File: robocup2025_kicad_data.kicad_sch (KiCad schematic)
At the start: 2 parts, among them U1 RASPBERRY_PI_4B_4GB, U2 ESP32-DEVKITC-32E

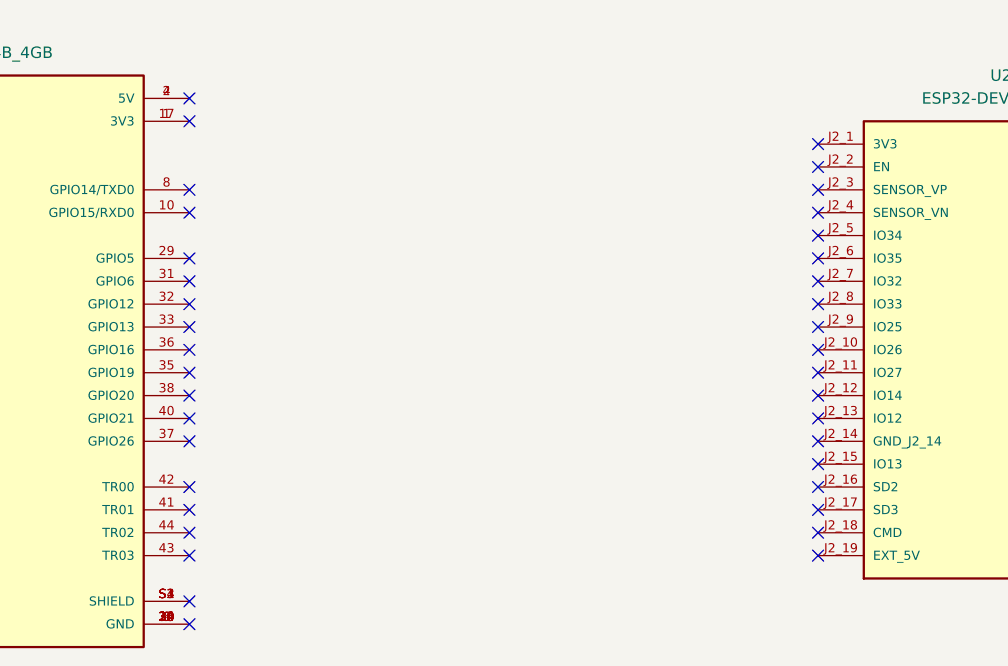
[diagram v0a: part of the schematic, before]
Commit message: robocup2025_kicad_data.kicad_sch: End of the day
ERC Failing
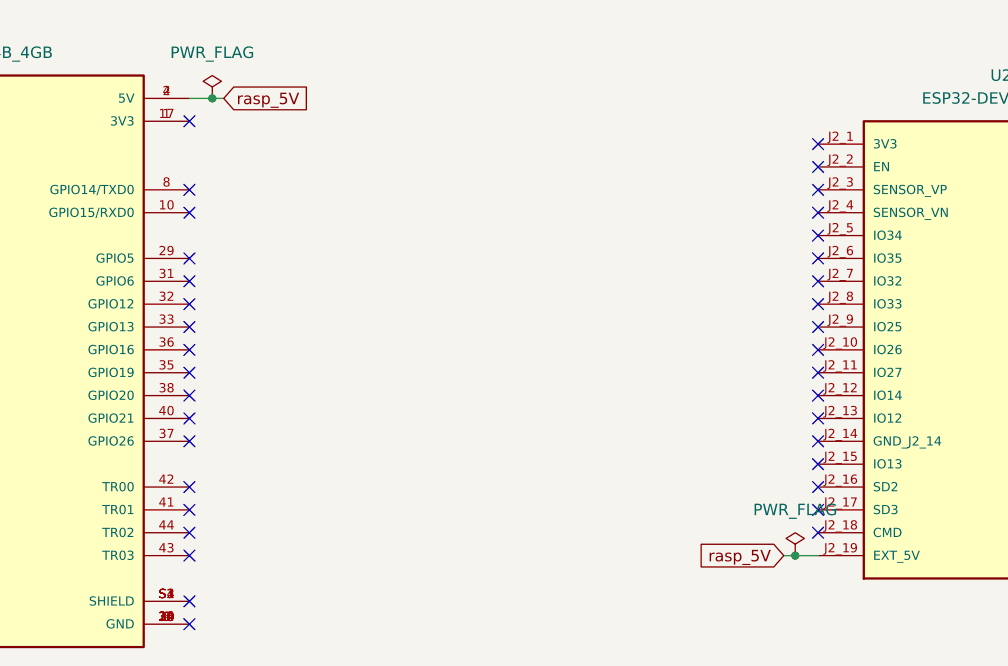
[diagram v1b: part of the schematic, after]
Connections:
- net rasp_5V: now reaches U1.2 (5V), U1.4 (5V)
- net rasp_5V: now also U2.J2_19 (EXT_5V)
- no-connect marks 70 -> 68
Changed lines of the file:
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@@
 	(generator_version "8.0")
 	(paper "A4")
+	(junction
+		(at 147.32 83.82)
+		(diameter 0)
+		(color 0 0 0 0)
+	)
+	(junction
+		(at 82.55 33.02)
+		(diameter 0)
+		(color 0 0 0 0)
+	)
 	(no_connect
 		(at 80.01 66.04)
@@
 	)
 	(no_connect
-		(at 149.86 83.82)
-	)
-	(no_connect
 		(at 80.01 35.56)
 	)
@@
 	(no_connect
 		(at 80.01 58.42)
-	)
-	(no_connect
-		(at 80.01 33.02)
 	)
 	(no_connect
@@
 	(wire
 		(pts
-			(xy 25.4 38.1) (xy 29.21 38.1)
+			(xy 82.55 33.02) (xy 83.82 33.02)
 		)
 		(stroke
@@
 	(wire
 		(pts
-			(xy 190.5 43.18) (xy 194.31 43.18)
+			(xy 25.4 38.1) (xy 29.21 38.1)
 		)
 		(stroke
 			(width 0)
 			(type default)
+		)
+	)
+	(wire
+		(pts
+			(xy 146.05 83.82) (xy 147.32 83.82)
+		)
+		(stroke
+			(width 0)
+			(type default)
+		)
+	)
+	(wire
+		(pts
+			(xy 190.5 43.18) (xy 194.31 43.18)
+		)
+		(stroke
+			(width 0)
+			(type default)
+		)
+	)
+	(wire
+		(pts
+			(xy 147.32 83.82) (xy 149.86 83.82)
+		)
+		(stroke
+			(width 0)
+			(type default)
+		)
+	)
+	(wire
+		(pts
+			(xy 80.01 33.02) (xy 82.55 33.02)
+		)
+		(stroke
+			(width 0)
+			(type default)
+		)
+	)
+	(global_label "rasp_5V"
+		(shape input)
+		(at 146.05 83.82 180)
+		(fields_autoplaced yes)
+		(effects
+			(font
+				(size 1.27 1.27)
+			)
+			(justify right)
+		)
+		(property "Intersheetrefs" "${INTERSHEET_REFS}"
+			(at 135.6868 83.82 0)
+			(effects
+				(font
+					(size 1.27 1.27)
+				)
+				(justify right)
+				(hide yes)
+			)
+		)
+	)
+	(global_label "rasp_5V"
+		(shape input)
+		(at 83.82 33.02 0)
+		(fields_autoplaced yes)
+		(effects
+			(font
+				(size 1.27 1.27)
+			)
+			(justify left)
+		)
+		(property "Intersheetrefs" "${INTERSHEET_REFS}"
+			(at 94.1832 33.02 0)
+			(effects
+				(font
+					(size 1.27 1.27)
+				)
+				(justify left)
+				(hide yes)
+			)
 		)
 	)
@@
 				(justify right)
 				(hide yes)
+			)
+		)
+	)
+	(symbol
+		(lib_id "power:PWR_FLAG")
+		(at 147.32 83.82 0)
+		(unit 1)
+		(exclude_from_sim no)
+		(in_bom yes)
+		(on_board yes)
+		(dnp no)
+		(fields_autoplaced yes)
+		(property "Reference" "#FLG2"
+			(at 147.32 81.915 0)
+			(effects
+				(font
+					(size 1.27 1.27)
+				)
+				(hide yes)
+			)
+		)
+		(property "Value" "PWR_FLAG"
+			(at 147.32 78.74 0)
+			(effects
+				(font
+					(size 1.27 1.27)
+				)
+			)
+		)
+		(property "Footprint" ""
+			(at 147.32 83.82 0)
+			(effects
+				(font
+					(size 1.27 1.27)
+				)
+				(hide yes)
+			)
+		)
+		(property "Datasheet" "~"
+			(at 147.32 83.82 0)
+			(effects
+				(font
+					(size 1.27 1.27)
+				)
+				(hide yes)
+			)
+		)
+		(property "Description" "Special symbol for telling ERC where power comes from"
+			(at 147.32 83.82 0)
+			(effects
+				(font
+					(size 1.27 1.27)
+				)
+				(hide yes)
+			)
+		)
+		(pin "1"
+		)
+		(instances
+			(project ""
+				(path "/c41ae4e6-c818-4751-9662-d6273ae109e5"
+					(reference "#FLG2")
+					(unit 1)
+				)
 			)
 		)
@@
 					(unit 1)
 				)
+			)
+		)
+	)
+	(symbol
+		(lib_id "power:PWR_FLAG")
+		(at 82.55 33.02 0)
+		(unit 1)
+		(exclude_from_sim no)
+		(in_bom yes)
+		(on_board yes)
+		(dnp no)
+		(fields_autoplaced yes)
+		(property "Reference" "#FLG1"
+			(at 82.55 31.115 0)
+			(effects
+				(font
+					(size 1.27 1.27)
+				)
+				(hide yes)
+			)
+		)
+		(property "Value" "PWR_FLAG"
+			(at 82.55 27.94 0)
+			(effects
+				(font
+					(size 1.27 1.27)
+				)
+			)
+		)
+		(property "Footprint" ""
+			(at 82.55 33.02 0)
+			(effects
+				(font
+					(size 1.27 1.27)
+				)
+				(hide yes)
+			)
+		)
+		(property "Datasheet" "~"
+			(at 82.55 33.02 0)
+			(effects
+				(font
+					(size 1.27 1.27)
+				)
+				(hide yes)
+			)
+		)
+		(property "Description" "Special symbol for telling ERC where power comes from"
+			(at 82.55 33.02 0)
+			(effects
+				(font
+					(size 1.27 1.27)
+				)
+				(hide yes)
+			)
+		)
+		(pin "1"
+		)
+		(instances
+			(project ""
+				(path "/c41ae4e6-c818-4751-9662-d6273ae109e5"
+					(reference "#FLG1")
+					(unit 1)
+				)

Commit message: robocup2025_kicad_data.kicad_sch: Placed servo motor
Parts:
- added M1, M2, M3, M4, M5: ~, symbol robo:servo_motor

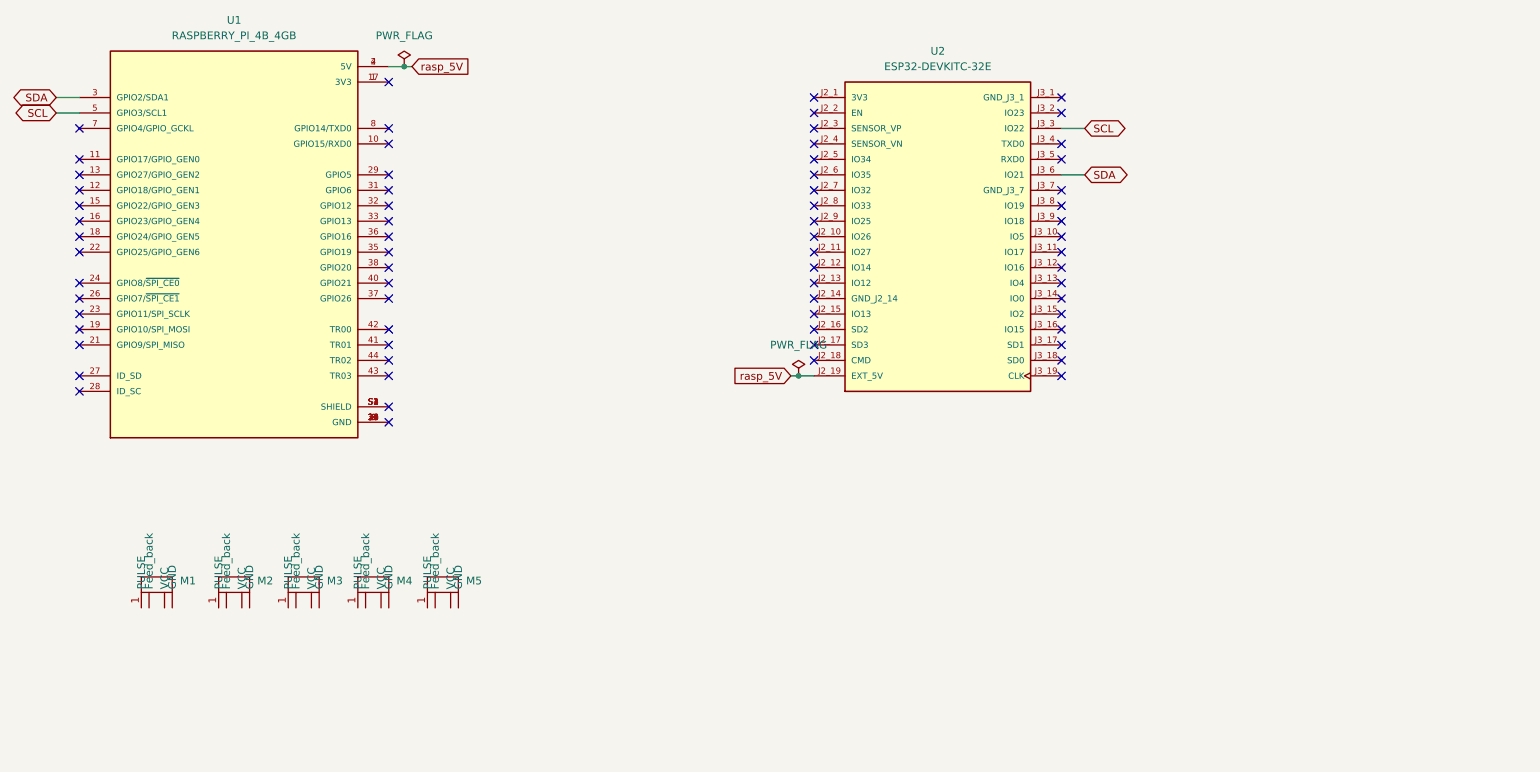
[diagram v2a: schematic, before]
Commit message: robocup2025_kicad_data.kicad_sch: Created servo motor
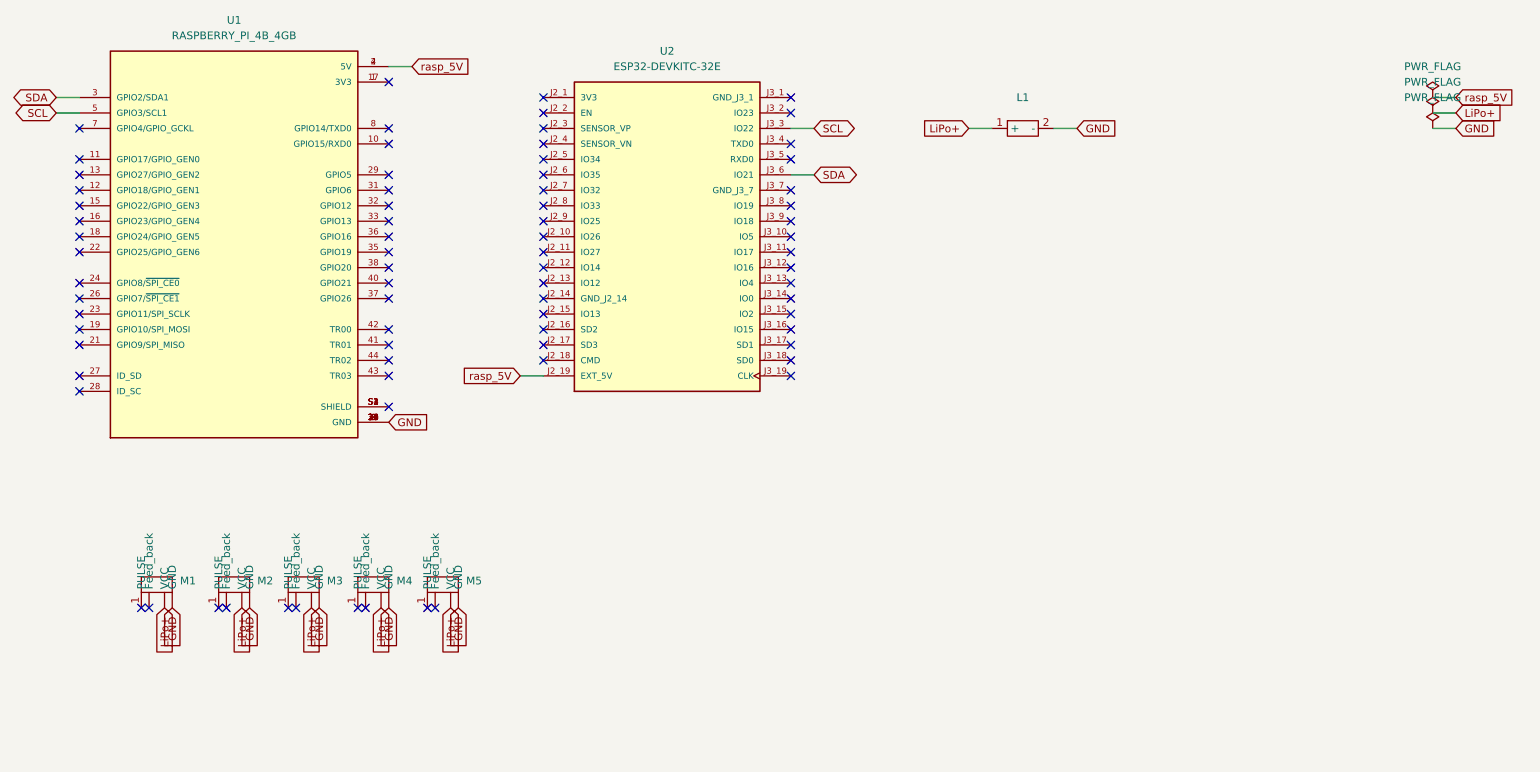
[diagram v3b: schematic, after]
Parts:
- added L1: ~, symbol robo:LiPo_battery
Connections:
- net GND: now reaches U1.14 (GND), U1.20 (GND), U1.25 (GND), U1.30 (GND), U1.34 (GND), U1.39 (GND), U1.6 (GND), U1.9 (GND)
- net GND: now also M1. (VCC), M2. (VCC), M3. (VCC), M4. (VCC), M5. (VCC), L1.2 (-)
- net LiPo+: now reaches M5. (VCC)
- net LiPo+: now also M1. (VCC), M2. (VCC), M3. (VCC), M4. (VCC), L1.1 (+)
- no-connect marks 68 -> 77
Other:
- moved on the sheet: U2

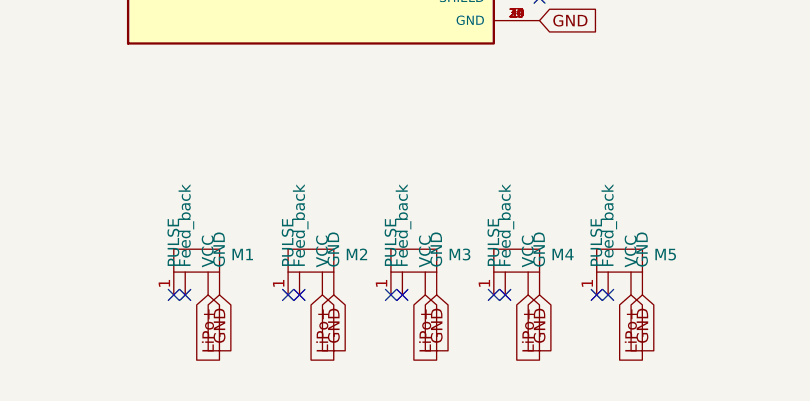
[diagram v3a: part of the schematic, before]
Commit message: robocup2025_kicad_data.kicad_prl,robocup2025_kicad_data.kicad_pro robocup2025_kicad_data.kicad_sch: Fixed servomotor pin number
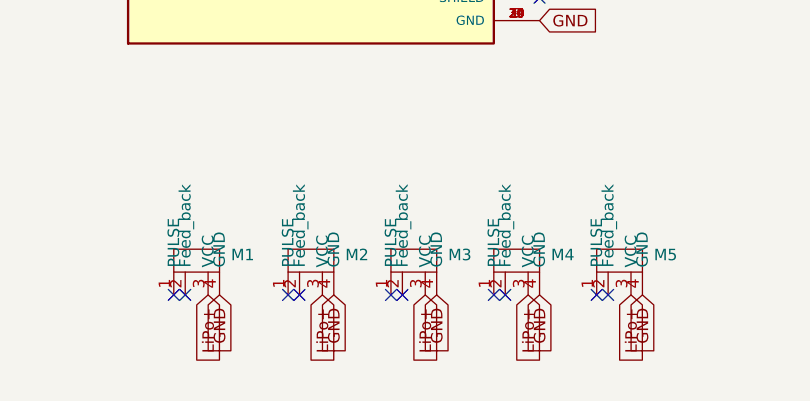
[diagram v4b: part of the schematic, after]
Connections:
- net GND: now also M1.4 (GND), M2.4 (GND), M3.4 (GND), M4.4 (GND), M5.4 (GND); no longer M1. (VCC), M2. (VCC), M3. (VCC), M4. (VCC), M5. (VCC)
- net LiPo+: now also M1.3 (VCC), M2.3 (VCC), M3.3 (VCC), M4.3 (VCC), M5.3 (VCC); no longer M1. (VCC), M2. (VCC), M3. (VCC), M4. (VCC), M5. (VCC)
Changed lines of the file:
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@@
 (kicad_sch
-	(version 20231120)
+	(version 20250114)
 	(generator "eeschema")
-	(generator_version "8.0")
+	(generator_version "9.0")
 	(paper "A4")
 	(no_connect
@@
 	)
 	(symbol
-		(lib_id "robo:servo_motor")
-		(at 41.91 118.11 0)
-		(unit 1)
-		(exclude_from_sim no)
-		(in_bom yes)
-		(on_board yes)
-		(dnp no)
-		(fields_autoplaced yes)
-		(property "Reference" "M1"
-			(at 45.72 117.4749 0)
-			(effects
-				(font
-					(size 1.27 1.27)
-				)
-				(justify left)
-			)
-		)
-		(property "Value" "~"
-			(at 45.72 119.38 0)
-			(effects
-				(font
-					(size 1.27 1.27)
-				)
-				(justify left)
-			)
-		)
-		(property "Footprint" ""
-			(at 41.91 118.11 0)
-			(effects
-				(font
-					(size 1.27 1.27)
-				)
-				(hide yes)
-			)
-		)
-		(property "Datasheet" ""
-			(at 41.91 118.11 0)
-			(effects
-				(font
-					(size 1.27 1.27)
-				)
-				(hide yes)
-			)
-		)
-		(property "Description" ""
-			(at 41.91 118.11 0)
-			(effects
-				(font
-					(size 1.27 1.27)
-				)
-				(hide yes)
-			)
-		)
-		(pin ""
-		)
-		(pin ""
-		)
-		(pin "1"
-		)
-		(pin ""
-		)
-		(instances
-			(project ""
-				(path "/c41ae4e6-c818-4751-9662-d6273ae109e5"
-					(reference "M1")
-					(unit 1)
-				)
-			)
-		)
-	)
-	(symbol
 		(lib_id "robo:RASPBERRY_PI_4B_4GB")
 		(at 54.61 63.5 0)
@@
 	)
 	(symbol
-		(lib_name "robo:servo_motor")
 		(lib_id "robo:servo_motor")
-		(at 88.9 118.11 0)
+		(at 54.61 118.11 0)
 		(unit 1)
 		(exclude_from_sim no)
@@
 		(dnp no)
 		(fields_autoplaced yes)
-		(property "Reference" "M5"
-			(at 92.71 117.4749 0)
+		(property "Reference" "M2"
+			(at 58.42 117.4749 0)
 			(effects
 				(font
@@
 		)
 		(property "Value" "~"
-			(at 92.71 119.38 0)
+			(at 58.42 119.38 0)
 			(effects
 				(font
@@
 		)
 		(property "Footprint" ""
-			(at 88.9 118.11 0)
+			(at 54.61 118.11 0)
 			(effects
 				(font
@@
 		)
 		(property "Datasheet" ""
-			(at 88.9 118.11 0)
+			(at 54.61 118.11 0)
 			(effects
 				(font
@@
 		)
 		(property "Description" ""
-			(at 88.9 118.11 0)
-			(effects
-				(font
-					(size 1.27 1.27)
-				)
-				(hide yes)
-			)
+			(at 54.61 118.11 0)
+			(effects
+				(font
+					(size 1.27 1.27)
+				)
+				(hide yes)
+			)
+		)
+		(pin "2"
 		)
 		(pin "1"
 		)
-		(pin ""
-		)
-		(pin ""
-		)
-		(pin ""
+		(pin "4"
+		)
+		(pin "3"
 		)
 		(instances
-			(project ""
+			(project "robocup2025_kicad_data"
 				(path "/c41ae4e6-c818-4751-9662-d6273ae109e5"
-					(reference "M5")
+					(reference "M2")
 					(unit 1)
 				)
@@
 	)
 	(symbol
-		(lib_name "robo:servo_motor")
 		(lib_id "robo:servo_motor")
 		(at 66.04 118.11 0)
@@
 			)
 		)
-		(pin ""
-		)
-		(pin ""
-		)
-		(pin ""
+		(pin "2"
 		)
 		(pin "1"
 		)
+		(pin "4"
+		)
+		(pin "3"
+		)
 		(instances
-			(project ""
+			(project "robocup2025_kicad_data"
 				(path "/c41ae4e6-c818-4751-9662-d6273ae109e5"
 					(reference "M3")
@@
 	)
 	(symbol
-		(lib_name "robo:servo_motor")
 		(lib_id "robo:servo_motor")
 		(at 77.47 118.11 0)
@@
 			)
 		)
+		(pin "2"
+		)
 		(pin "1"
 		)
-		(pin ""
-		)
-		(pin ""
-		)
-		(pin ""
+		(pin "4"
+		)
+		(pin "3"
 		)
 		(instances
-			(project ""
+			(project "robocup2025_kicad_data"
 				(path "/c41ae4e6-c818-4751-9662-d6273ae109e5"
 					(reference "M4")
@@
 	)
 	(symbol
-		(lib_name "robo:servo_motor")
 		(lib_id "robo:servo_motor")
-		(at 54.61 118.11 0)
+		(at 88.9 118.11 0)
 		(unit 1)
 		(exclude_from_sim no)
@@
 		(dnp no)
 		(fields_autoplaced yes)
-		(property "Reference" "M2"
-			(at 58.42 117.4749 0)
+		(property "Reference" "M5"
+			(at 92.71 117.4749 0)
 			(effects
 				(font
@@
 		)
 		(property "Value" "~"
-			(at 58.42 119.38 0)
+			(at 92.71 119.38 0)
 			(effects
 				(font
@@
 		)
 		(property "Footprint" ""
-			(at 54.61 118.11 0)
+			(at 88.9 118.11 0)
 			(effects
 				(font
@@
 		)
 		(property "Datasheet" ""
-			(at 54.61 118.11 0)
+			(at 88.9 118.11 0)
 			(effects
 				(font
@@
 		)
 		(property "Description" ""
-			(at 54.61 118.11 0)
-			(effects
-				(font
-					(size 1.27 1.27)
-				)
-				(hide yes)
-			)
+			(at 88.9 118.11 0)
+			(effects
+				(font
+					(size 1.27 1.27)
+				)
+				(hide yes)
+			)
+		)
+		(pin "2"
 		)
 		(pin "1"
 		)
-		(pin ""
-		)
-		(pin ""
-		)
-		(pin ""
+		(pin "4"
+		)
+		(pin "3"
+		)
+		(instances
+			(project "robocup2025_kicad_data"
+				(path "/c41ae4e6-c818-4751-9662-d6273ae109e5"
+					(reference "M5")
+					(unit 1)
+				)
+			)
+		)
+	)
+	(symbol
+		(lib_id "robo:servo_motor")
+		(at 41.91 118.11 0)
+		(unit 1)
+		(exclude_from_sim no)
+		(in_bom yes)
+		(on_board yes)
+		(dnp no)
+		(fields_autoplaced yes)
+		(property "Reference" "M1"
+			(at 45.72 117.4749 0)
+			(effects
+				(font
+					(size 1.27 1.27)
+				)
+				(justify left)
+			)
+		)
+		(property "Value" "~"
+			(at 45.72 119.38 0)
+			(effects
+				(font
+					(size 1.27 1.27)
+				)
+				(justify left)
+			)
+		)
+		(property "Footprint" ""
+			(at 41.91 118.11 0)
+			(effects
+				(font
+					(size 1.27 1.27)
+				)
+				(hide yes)
+			)
+		)
+		(property "Datasheet" ""
+			(at 41.91 118.11 0)
+			(effects
+				(font
+					(size 1.27 1.27)
+				)
+				(hide yes)
+			)
+		)
+		(property "Description" ""
+			(at 41.91 118.11 0)
+			(effects
+				(font
+					(size 1.27 1.27)
+				)
+				(hide yes)
+			)
+		)
+		(pin "2"
+		)
+		(pin "1"
+		)
+		(pin "4"
+		)
+		(pin "3"
 		)
 		(instances
 			(project ""
 				(path "/c41ae4e6-c818-4751-9662-d6273ae109e5"
-					(reference "M2")
+					(reference "M1")
 					(unit 1)
 				)
@@
 		)
 	)
+	(embedded_fonts no)
 )

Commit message: robocup2025_kicad_data.kicad_sch: Connected servo motor to esp
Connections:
- net tyre_pulse_2: now reaches M2.1 (PULSE)
- net tyre_pulse_2: now also U2.J2_12 (IO14)
- net tyre_pulse_1: now reaches U2.J2_15 (IO13)
- net tyre_pulse_1: now also M1.1 (PULSE)
- net arm_feedback: now reaches U2.J2_5 (IO34)
- net arm_feedback: now also M5.2 (Feed_back)
- net arm_pulse: now reaches U2.J3_11 (IO17)
- net arm_pulse: now also M5.1 (PULSE)
- net tyre_pulse_4: now reaches U2.J3_12 (IO16)
- net tyre_pulse_4: now also M4.1 (PULSE)
- net tyre_pulse_3: now reaches U2.J3_16 (IO15)
- net tyre_pulse_3: now also M3.1 (PULSE)
- no-connect marks 77 -> 65
